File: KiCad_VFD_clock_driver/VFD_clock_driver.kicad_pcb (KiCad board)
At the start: 2 copper layers, 95 x 50 mm, 76 parts, among them J1 Barrel_Jack, J2 SWD, J3 Multiplexer, J4 Segments, J5 UART, M1 MountingHole_2.1mm, M2 MountingHole_2.1mm, M3 MountingHole_2.1mm, M4 MountingHole_2.1mm, M5 MountingHole_2.1mm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

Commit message: VFD tube power connector on BCB
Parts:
- added J6: VFD display power, Connector_PinSocket_2.54mm:PinSocket_1x04_P2.54mm_Vertical, F.Cu at (150.0, 97.0)
- RV1: renamed from VFD VOLTAGE
- moved G*** 2.31 mm to (218.2, 101.8)
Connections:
- U1 pad 4: (no net) -> Net-(U1-Pad4)
- U5 pad 3: (no net) -> Net-(U5-Pad3)
- U6 pad 25: (no net) -> Net-(U6-Pad25)
- U6 pad 3: (no net) -> Net-(U6-Pad3)
- U6 pad 32: (no net) -> Net-(U6-Pad32)
- U6 pad 33: (no net) -> Net-(U6-Pad33)
- U6 pad 38: (no net) -> Net-(U6-Pad38)
- U6 pad 4: (no net) -> Net-(U6-Pad4)
- U6 pad 6: (no net) -> Net-(U6-Pad6)
- U7 pad 10: (no net) -> Net-(U7-Pad10)
- U8 pad 10: (no net) -> Net-(U8-Pad10)
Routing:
- net /VIN: track 60.4 -> 74.7 mm
- net +3V3: track 260.0 -> 272.9 mm, vias 5 -> 6
- net GND: track 398.0 -> 408.7 mm
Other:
- board text added: "SWD"
- board text added: "UART"
- board text added: "VIN"

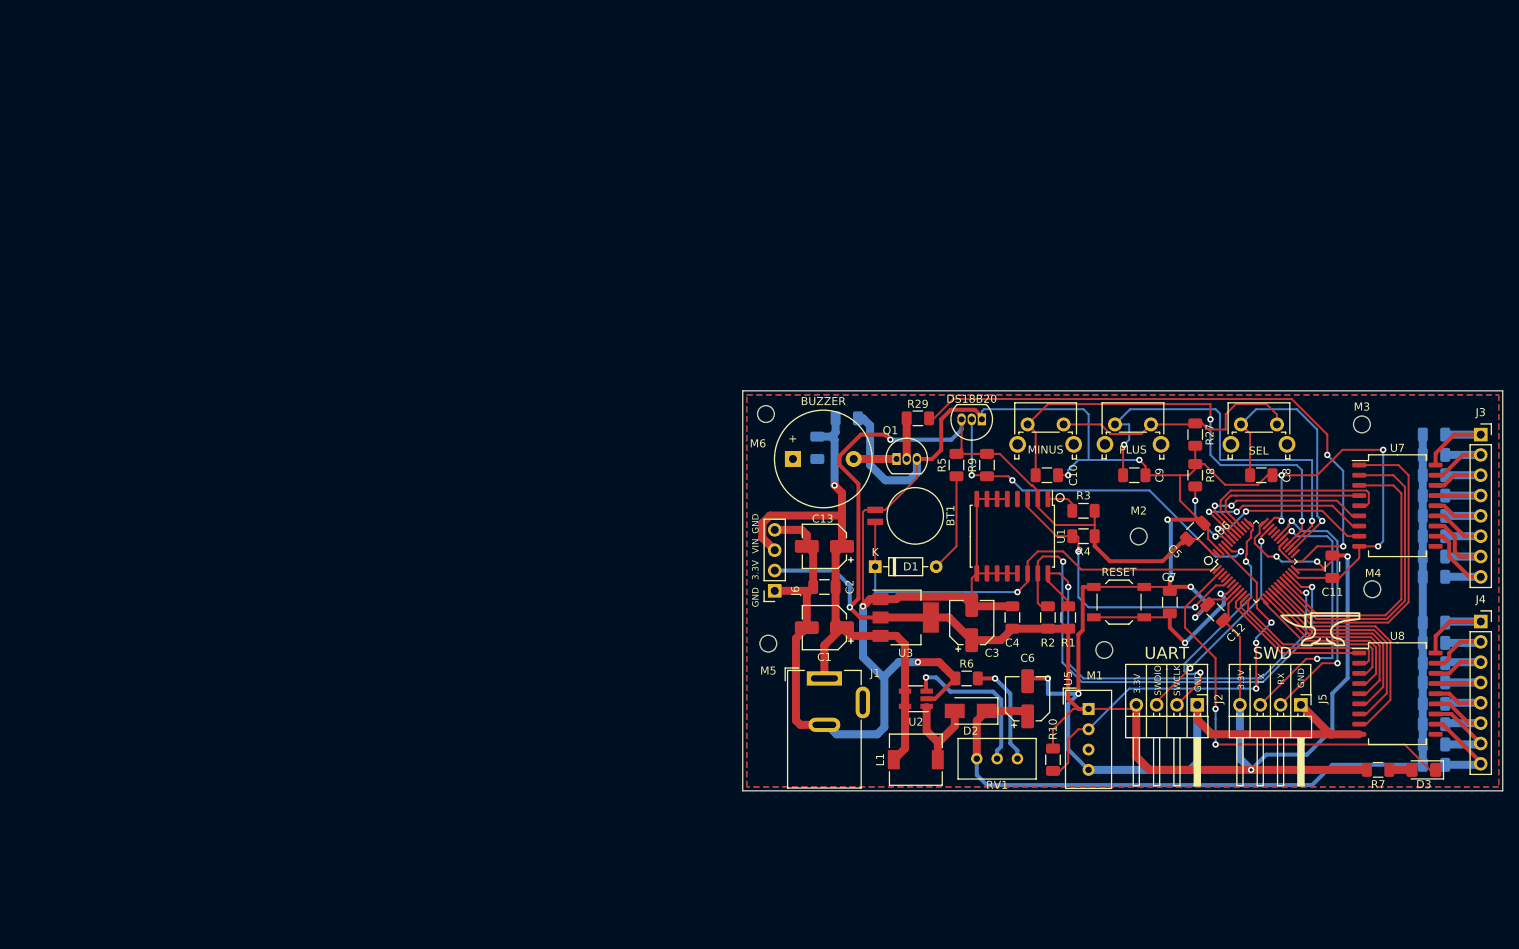
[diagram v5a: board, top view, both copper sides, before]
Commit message: External PCB for VFD tube and H-brigde
+ additional PCB for VFD tube with H-bridge
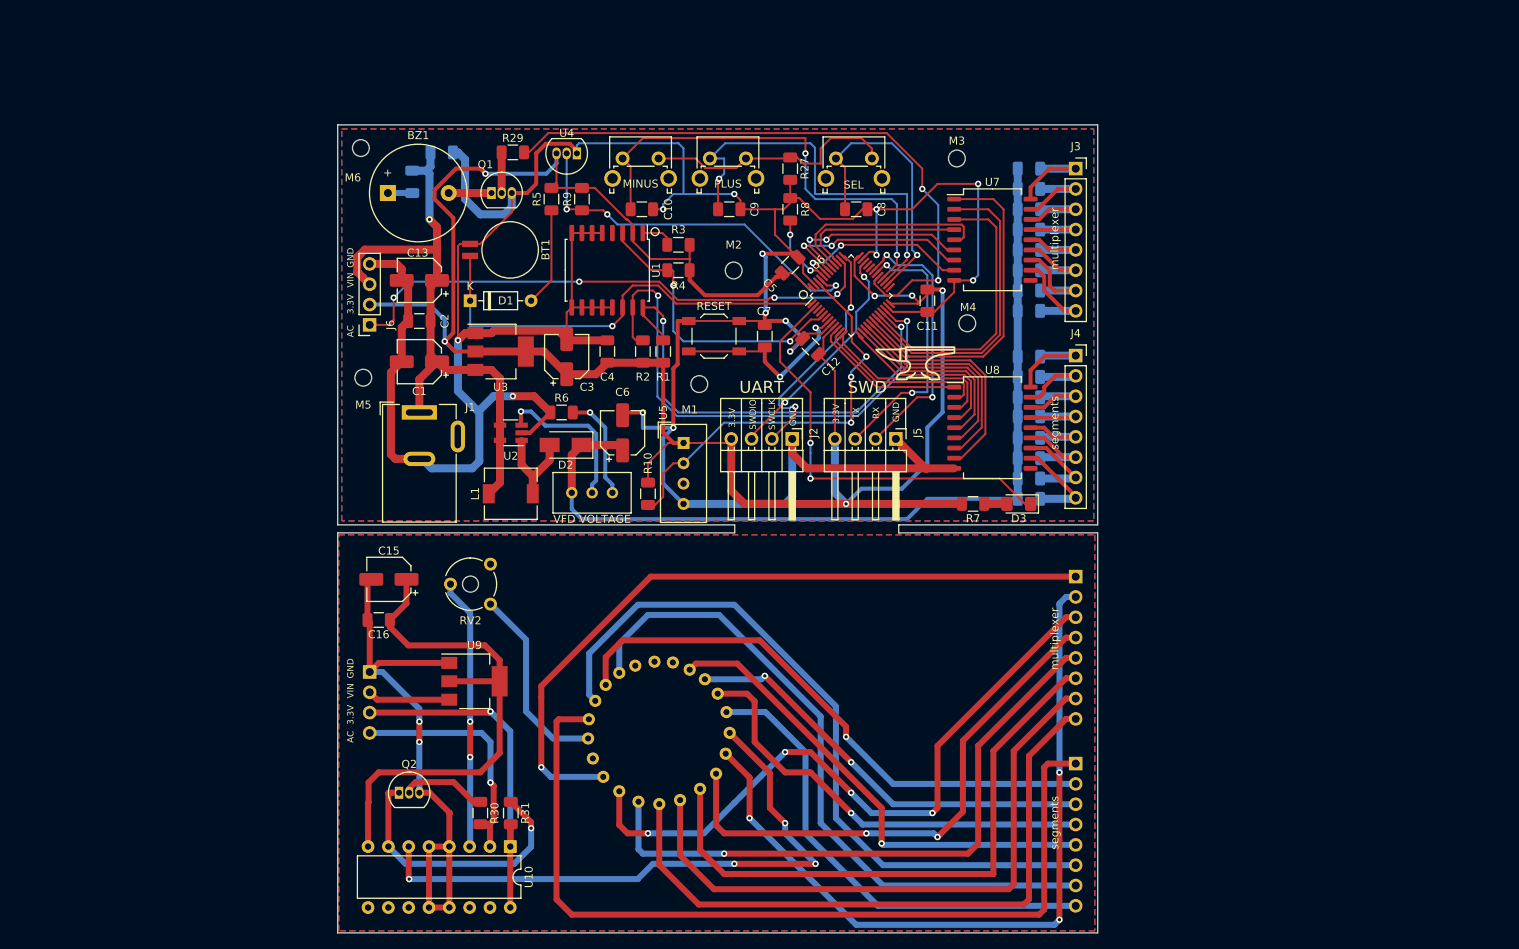
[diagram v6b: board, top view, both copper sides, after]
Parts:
- added C15: 47uF, Capacitor_SMD:CP_Elec_5x4.4, F.Cu at (101.8, 95.6)
- added C16: 100nF, Capacitor_SMD:C_1206_3216Metric, F.Cu at (100.5, 100.6)
- added G***: LOGO, WK_lib:Anvil_10x10mm, B.Cu at (127.9, 93.3)
- added J7: VFD display driver, Connector_PinHeader_2.54mm:PinHeader_1x04_P2.54mm_Vertical, B.Cu at (99.4, 107.1)
- added J8: Segments inputs, Connector_PinHeader_2.54mm:PinHeader_1x08_P2.54mm_Vertical, B.Cu at (187.6, 118.6)
- added J9: Multiplexer inputs, Connector_PinHeader_2.54mm:PinHeader_1x08_P2.54mm_Vertical, B.Cu at (187.6, 95.2)
- added Q2: BC547, Package_TO_SOT_THT:TO-92_Inline, F.Cu at (103.0, 122.2)
- added R30: 1K, Resistor_SMD:R_1206_3216Metric, F.Cu at (113.2, 124.8)
- added R31: 10K, Resistor_SMD:R_1206_3216Metric, F.Cu at (117.0, 124.8)
- added RV2: 1K, Potentiometer_THT:Potentiometer_Piher_PT-6-V_Vertical_Hole, F.Cu at (114.5, 93.7)
- added U10: L293, Package_DIP:DIP-16_W7.62mm, F.Cu at (116.9, 129.0)
- added U9: AMS1117-5.0, Package_TO_SOT_SMD:SOT-223-3_TabPin2, F.Cu at (112.5, 108.3)
- added VFD1: IV-18, WK_lib:IV-18, B.Cu at (135.4, 114.8)
- J6: value VFD display power -> VFD display driver
- VFD VOLTAGE: renamed from RV1
- moved C10 60.6 mm to (133.4, 49.3)
- moved C4 60.6 mm to (129.1, 67.1)
- moved C6 60.6 mm to (131.0, 77.2)
- moved MINUS 60.6 mm to (131.0, 43.0)
- moved PLUS 60.6 mm to (141.9, 43.0)
- moved R7 60.6 mm to (174.8, 86.1)
- moved U1 60.6 mm to (129.1, 56.9)
- moved C1 60.6 mm to (105.6, 68.4)
- moved C13 60.6 mm to (105.6, 58.2)
- moved C2 60.6 mm to (105.6, 63.3)
- moved J1 60.6 mm to (105.6, 74.7)
- moved M6 60.6 mm to (98.3, 41.7)
- moved Q1 60.6 mm to (114.6, 47.3)
- moved R29 60.6 mm to (117.3, 42.2)
- moved R6 60.6 mm to (123.4, 74.7)
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- renumbered BUZZER to BZ1, DS18B20 to U4
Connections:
- J6 pad 1: GND -> /VFD_AC
- U6 pad 38: Net-(U6-Pad38) -> /VFD_AC
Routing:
- net Net-(J8-Pad1): track 0.00 -> 110.3 mm
- net Net-(J9-Pad2): track 0.00 -> 95.7 mm, vias 0 -> 3
- net Net-(J8-Pad6): track 0.00 -> 91.3 mm
- net Net-(J9-Pad1): track 0.00 -> 90.9 mm, vias 0 -> 1
- net Net-(J8-Pad7): track 0.00 -> 84.0 mm
- net Net-(J9-Pad3): track 0.00 -> 83.7 mm, vias 0 -> 4
- net Net-(J9-Pad8): track 0.00 -> 81.8 mm
- net Net-(J9-Pad5): track 0.00 -> 78.1 mm, vias 0 -> 1
- net Net-(J9-Pad7): track 0.00 -> 77.7 mm
- net Net-(U10-Pad6): track 0.00 -> 76.5 mm, vias 0 -> 4
- net Net-(J9-Pad6): track 0.00 -> 75.0 mm
- net Net-(J8-Pad2): track 0.00 -> 71.3 mm, vias 0 -> 1
- net Net-(C15-Pad2): track 0.00 -> 70.3 mm, vias 0 -> 2
- net /VFD_AC: track 0.00 -> 68.5 mm, vias 0 -> 4
- net Net-(J9-Pad4): track 0.00 -> 67.5 mm, vias 0 -> 2
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- added copper zone on B.Cu, net Net-(C15-Pad2)
- added copper zone on F.Cu, net Net-(C15-Pad2)
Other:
- board size 95 x 50 mm -> 95 x 101 mm
- board text added: "AC"
- board text added: "JLCJLCJLCJLC"
- board text added: "VFD clock display"
- board text added: "multiplexer"
- board text added: "segments"

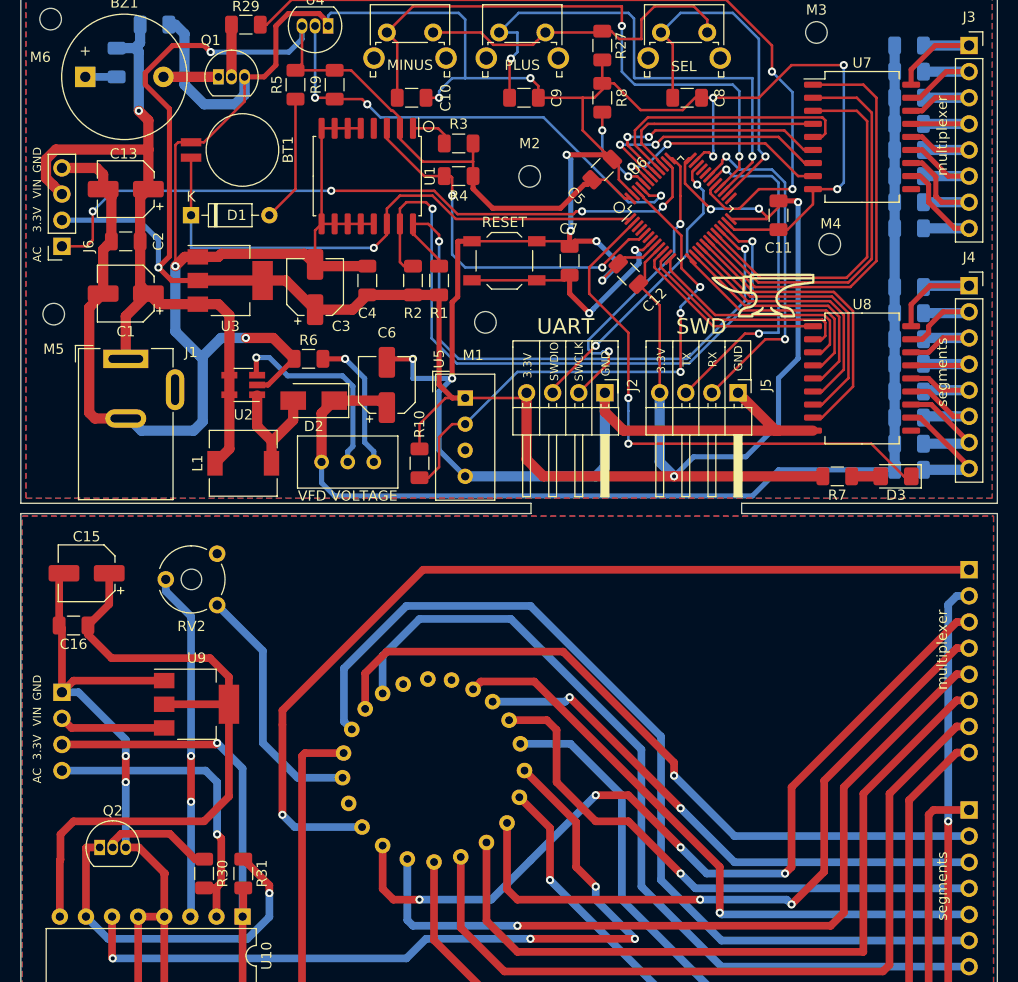
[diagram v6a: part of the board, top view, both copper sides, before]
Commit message: Mounting holes on tube PCB
+ added mounting holed on tube PCB, new holes are aligned with old ones in driver PCB
+ fixed misplaced UART and SWD connectors descriptions on silkscreen
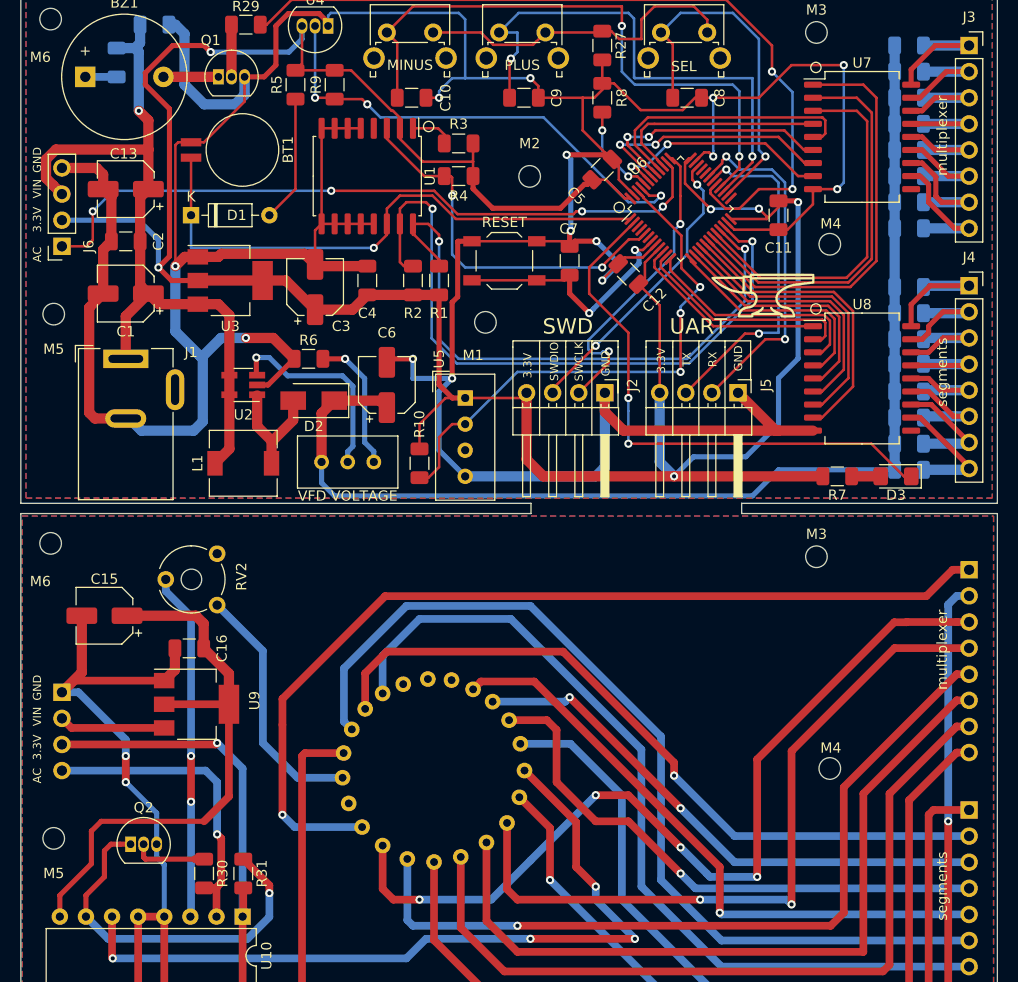
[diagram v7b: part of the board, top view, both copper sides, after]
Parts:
- added M3: MountingHole_2.1mm, MountingHole:MountingHole_2.1mm, F.Cu at (172.8, 94.0)
- added M4: MountingHole_2.1mm, MountingHole:MountingHole_2.1mm, F.Cu at (174.1, 114.6)
- added M5: MountingHole_2.1mm, MountingHole:MountingHole_2.1mm, F.Cu at (98.6, 121.4)
- added M6: MountingHole_2.1mm, MountingHole:MountingHole_2.1mm, F.Cu at (98.3, 92.7)
- moved C16 11.5 mm to (111.8, 102.9)
- moved C15 4.48 mm to (103.5, 99.7)
- moved Q2 3.02 mm to (106.0, 121.9)
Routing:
- net Net-(C15-Pad1): track 66.1 -> 56.3 mm
- net Net-(J9-Pad4): track 67.5 -> 71.1 mm
- net Net-(Q2-Pad2): track 10.8 -> 8.11 mm
- net Net-(J9-Pad3): track 83.7 -> 86.2 mm
- net Net-(Q2-Pad1): track 34.3 -> 36.3 mm
- net Net-(C15-Pad2): track 70.3 -> 69.4 mm
- net Net-(J9-Pad1): track 90.9 -> 91.5 mm

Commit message: Changes in footprints, changed VCC pin in SX1308
+ changed polarized capacitors footprints to biiger ones
+ changed SX1308 footprint to 6 legged version
+ changed logic VCC for L293 from 3.3V to 5V
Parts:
- C1, C13, C15, C3, C6: footprint Capacitor_SMD:CP_Elec_5x4.4 -> Capacitor_SMD:CP_Elec_6.3x4.5
- RV1: renamed from VFD VOLTAGE
- U2: footprint Package_TO_SOT_SMD:SOT-23-5_HandSoldering -> Package_TO_SOT_SMD:SOT-23-6_Handsoldering
- moved D1 1.57 mm to (113.5, 60.7)
- moved C13 1.45 mm to (107.0, 58.5)
- renumbered RESET to SW1, SEL to SW2, PLUS to SW3, MINUS to SW4
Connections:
- R31 pad 2: Net-(J7-Pad3) -> Net-(C15-Pad1)
- U10 pad 1: Net-(J7-Pad3) -> Net-(C15-Pad1)
- U10 pad 16: Net-(J7-Pad3) -> Net-(C15-Pad1)
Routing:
- net Net-(J7-Pad3): track 43.5 -> 0.00 mm, vias 1 -> 0
- net Net-(C15-Pad1): track 56.3 -> 82.0 mm
- net +3V3: track 272.5 -> 261.0 mm, vias 6 -> 8
- net /VIN: track 74.7 -> 84.8 mm
- net /VFD_AC: track 68.5 -> 70.1 mm
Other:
- board text added: "MINUS"
- board text added: "PLUS"
- board text added: "RESET"
- board text added: "SELECT"
